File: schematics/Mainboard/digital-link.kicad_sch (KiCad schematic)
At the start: 1 part, among them J5 PCIE-036-02-X-D-TH

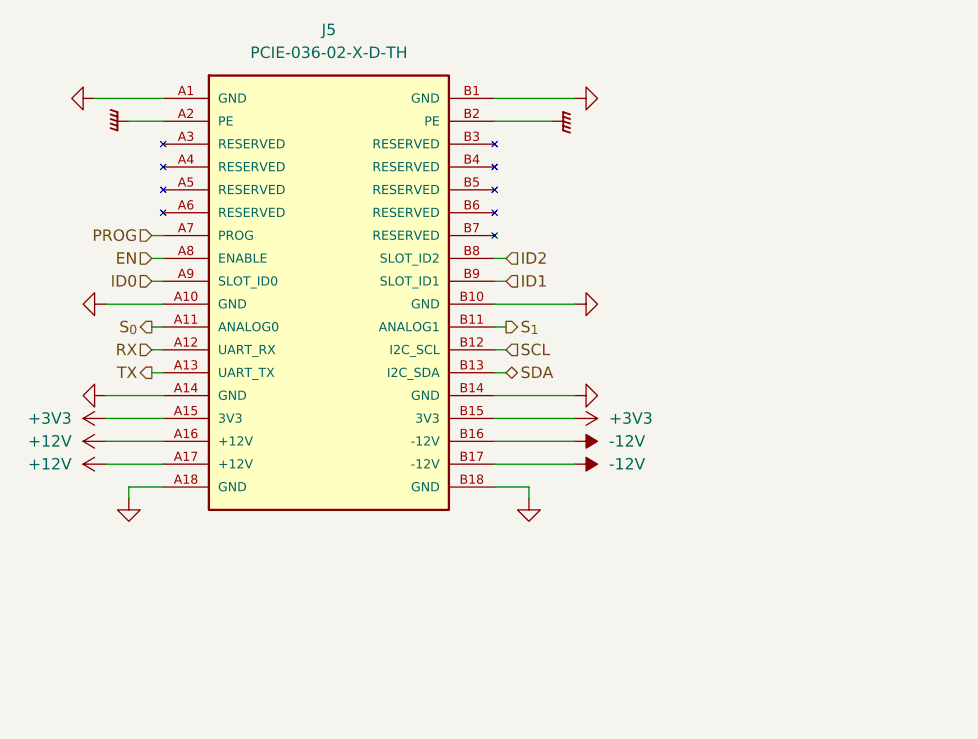
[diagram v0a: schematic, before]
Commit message: feat(mainboard): Added MCU and link comm bus
Signed-off-by: Andrew Balmos <abalmos@purdue.edu>
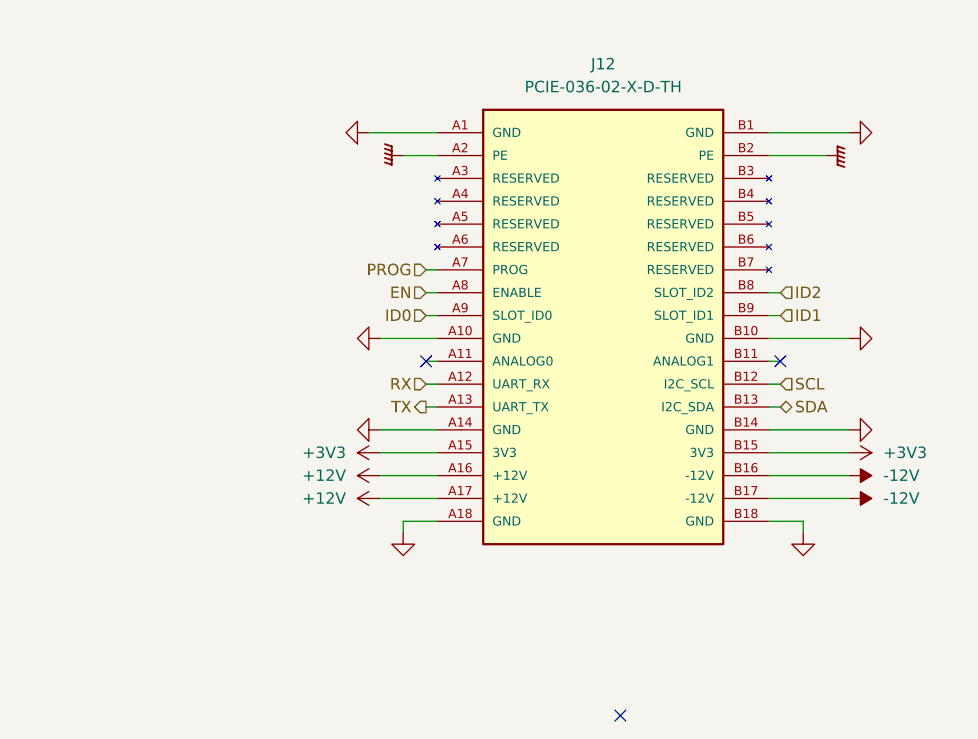
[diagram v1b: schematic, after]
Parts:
- removed J5: PCIE-036-02-X-D-TH, PCIE-036-02-X-D-TH:SAMTEC_PCIE-036-02-X-D-TH, symbol link-components:link-edge-connector
- added J12: PCIE-036-02-X-D-TH, PCIE-036-02-X-D-TH:SAMTEC_PCIE-036-02-X-D-TH, symbol link-components:link-edge-connector
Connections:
- net +12V: now also J12.A16 (+12V), J12.A17 (+12V)
- net +3V3: now also J12.A15 (3V3), J12.B15 (3V3)
- net -12V: now also J12.B16 (-12V), J12.B17 (-12V)
- net EN: now also J12.A8 (ENABLE)
- net GND: now also J12.A1 (GND), J12.A10 (GND), J12.A14 (GND), J12.A18 (GND), J12.B1 (GND), J12.B10 (GND), J12.B14 (GND), J12.B18 (GND)
- net GNDPWR: now also J12.A2 (PE), J12.B2 (PE)
- net ID0: now also J12.A9 (SLOT_ID0)
- net ID1: now also J12.B9 (SLOT_ID1)
- net ID2: now also J12.B8 (SLOT_ID2)
- net PROG: now also J12.A7 (PROG)
- net RX: now also J12.A12 (UART_RX)
- net SCL: now also J12.B12 (I2C_SCL)
- net SDA: now also J12.B13 (I2C_SDA)
- net TX: now also J12.A13 (UART_TX)
- no-connect marks 0 -> 3

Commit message: bug(labels): Fixed some incorrect labels
Signed-off-by: Andrew Balmos <abalmos@purdue.edu>
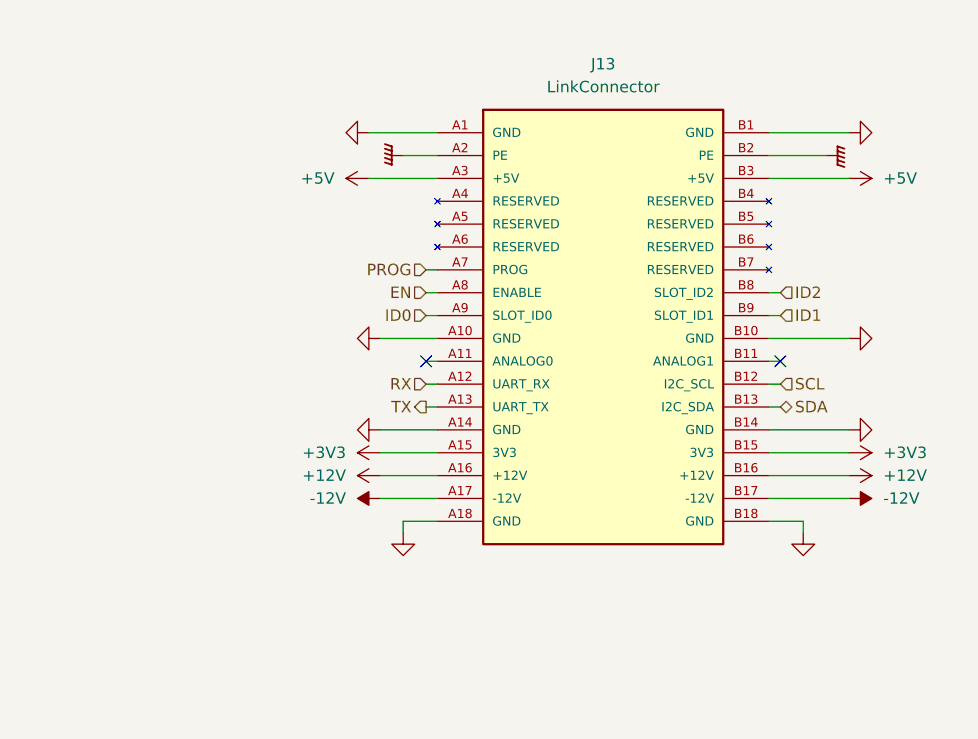
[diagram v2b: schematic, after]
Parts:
- J13: renamed from J12; value PCIE-036-02-X-D-TH -> LinkConnector
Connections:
- net +12V: now also J13.B16 (+12V); no longer J13.A17 (+12V)
- net -12V: now also J13.A17 (-12V); no longer J13.B16 (-12V)
- net +5V: now reaches J13.A3 (+5V)
- net +5V: now also J13.B3 (+5V)
- no-connect marks 3 -> 2

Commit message: bug(pcb): Link connector updates
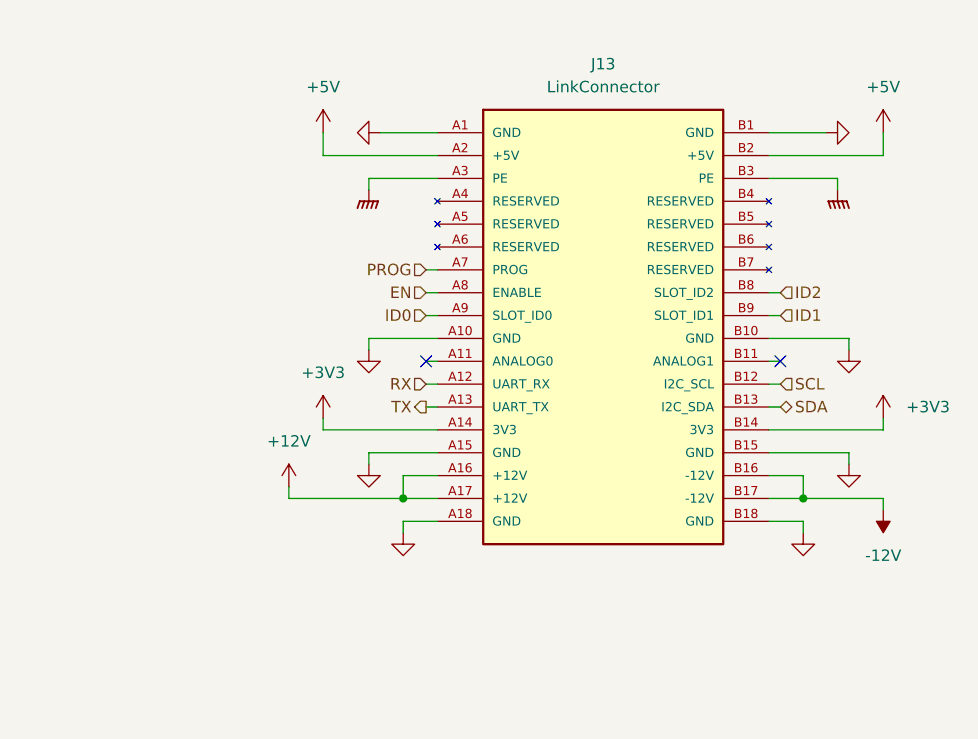
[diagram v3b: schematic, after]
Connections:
- net +12V: now also J13.A17 (+12V); no longer J13.B16 (+12V)
- net +3V3: now also J13.A14 (3V3), J13.B14 (3V3); no longer J13.A15 (3V3), J13.B15 (3V3)
- net +5V: now also J13.A2 (+5V), J13.B2 (+5V); no longer J13.A3 (+5V), J13.B3 (+5V)
- net -12V: now also J13.B16 (-12V); no longer J13.A17 (-12V)
- net GND: now also J13.A15 (GND), J13.B15 (GND); no longer J13.A14 (GND), J13.B14 (GND)
- net GNDPWR: now also J13.A3 (PE), J13.B3 (PE); no longer J13.A2 (PE), J13.B2 (PE)

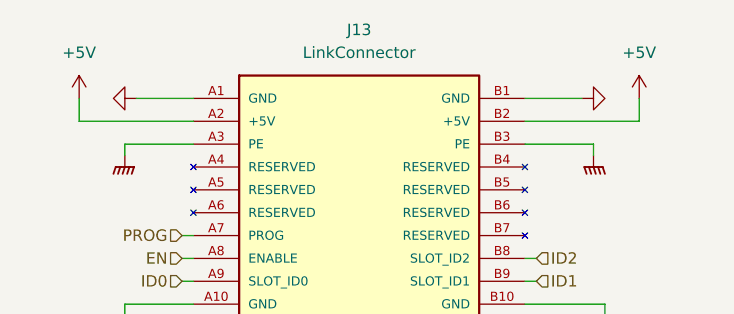
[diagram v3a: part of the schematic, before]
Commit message: feat(mainboard): Finished mainboard part selection
Signed-off-by: Andrew Balmos <abalmos@purdue.edu>
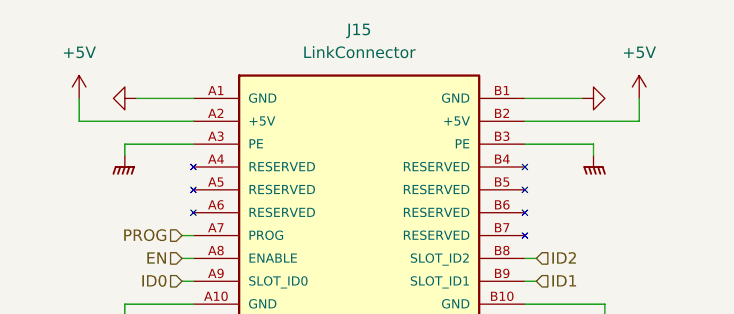
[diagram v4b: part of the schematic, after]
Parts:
- J15: renamed from J13; footprint PCIE-036-02-X-D-TH:SAMTEC_PCIE-036-02-X-D-TH -> Link_Footprints:SAMTEC_PCIE-036-02-X-D-TH; DigiKey (none) -> SAM10625-ND; LCSC (none) -> C194068; MPN (none) -> PCIE-036-02-F-D-TH
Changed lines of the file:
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@@
 		(dnp no)
 		(fields_autoplaced yes)
-		(property "Reference" "#PWR0171"
+		(property "Reference" "#PWR0213"
 			(at 116.84 100.33 0)
 			(effects
@@
 			(project "Mainboard"
 				(path "/95469dea-851e-4724-988e-7a6acaa4cbf0/4d738d37-6463-438f-b983-18ca4c02b52a"
-					(reference "#PWR0171")
+					(reference "#PWR0213")
 					(unit 1)
 				)
@@
 		(dnp no)
 		(fields_autoplaced yes)
-		(property "Reference" "#PWR0195"
+		(property "Reference" "#PWR0224"
 			(at 179.07 68.58 0)
 			(effects
@@
 			(project "Mainboard"
 				(path "/95469dea-851e-4724-988e-7a6acaa4cbf0/4d738d37-6463-438f-b983-18ca4c02b52a"
-					(reference "#PWR0195")
+					(reference "#PWR0224")
 					(unit 1)
 				)
@@
 		(dnp no)
 		(fields_autoplaced yes)
-		(property "Reference" "#PWR0190"
+		(property "Reference" "#PWR0222"
 			(at 175.26 95.25 0)
 			(effects
@@
 			(project "Mainboard"
 				(path "/95469dea-851e-4724-988e-7a6acaa4cbf0/4d738d37-6463-438f-b983-18ca4c02b52a"
-					(reference "#PWR0190")
+					(reference "#PWR0222")
 					(unit 1)
 				)
@@
 		(dnp no)
 		(fields_autoplaced yes)
-		(property "Reference" "#PWR0177"
+		(property "Reference" "#PWR0216"
 			(at 121.92 107.95 0)
 			(effects
@@
 			(project "Mainboard"
 				(path "/95469dea-851e-4724-988e-7a6acaa4cbf0/4d738d37-6463-438f-b983-18ca4c02b52a"
-					(reference "#PWR0177")
+					(reference "#PWR0216")
 					(unit 1)
 				)
@@
 		(dnp no)
 		(fields_autoplaced yes)
-		(property "Reference" "#PWR0188"
+		(property "Reference" "#PWR0220"
 			(at 179.07 64.77 0)
 			(effects
@@
 			(project "Mainboard"
 				(path "/95469dea-851e-4724-988e-7a6acaa4cbf0/4d738d37-6463-438f-b983-18ca4c02b52a"
-					(reference "#PWR0188")
+					(reference "#PWR0220")
 					(unit 1)
 				)
@@
 		(dnp no)
 		(fields_autoplaced yes)
-		(property "Reference" "#PWR0184"
+		(property "Reference" "#PWR0219"
 			(at 170.18 115.57 0)
 			(effects
@@
 			(project "Mainboard"
 				(path "/95469dea-851e-4724-988e-7a6acaa4cbf0/4d738d37-6463-438f-b983-18ca4c02b52a"
-					(reference "#PWR0184")
+					(reference "#PWR0219")
 					(unit 1)
 				)
@@
 		(dnp no)
 		(fields_autoplaced yes)
-		(property "Reference" "#PWR0196"
+		(property "Reference" "#PWR0225"
 			(at 179.07 100.33 0)
 			(effects
@@
 			(project "Mainboard"
 				(path "/95469dea-851e-4724-988e-7a6acaa4cbf0/4d738d37-6463-438f-b983-18ca4c02b52a"
-					(reference "#PWR0196")
+					(reference "#PWR0225")
 					(unit 1)
 				)
@@
 		(dnp no)
 		(fields_autoplaced yes)
-		(property "Reference" "#PWR0170"
+		(property "Reference" "#PWR0212"
 			(at 116.84 68.58 0)
 			(effects
@@
 			(project "Mainboard"
 				(path "/95469dea-851e-4724-988e-7a6acaa4cbf0/4d738d37-6463-438f-b983-18ca4c02b52a"
-					(reference "#PWR0170")
+					(reference "#PWR0212")
 					(unit 1)
 				)
@@
 		(dnp no)
 		(fields_autoplaced yes)
-		(property "Reference" "#PWR0194"
+		(property "Reference" "#PWR0223"
 			(at 175.26 107.95 0)
 			(effects
@@
 			(project "Mainboard"
 				(path "/95469dea-851e-4724-988e-7a6acaa4cbf0/4d738d37-6463-438f-b983-18ca4c02b52a"
-					(reference "#PWR0194")
+					(reference "#PWR0223")
 					(unit 1)
 				)
@@
 		(dnp no)
 		(fields_autoplaced yes)
-		(property "Reference" "#PWR0183"
+		(property "Reference" "#PWR0218"
 			(at 125.73 115.57 0)
 			(effects
@@
 			(project "Mainboard"
 				(path "/95469dea-851e-4724-988e-7a6acaa4cbf0/4d738d37-6463-438f-b983-18ca4c02b52a"
-					(reference "#PWR0183")
+					(reference "#PWR0218")
 					(unit 1)
 				)
@@
 		(dnp no)
 		(fields_autoplaced yes)
-		(property "Reference" "#PWR0172"
+		(property "Reference" "#PWR0214"
 			(at 121.92 76.2 0)
 			(effects
@@
 			(project "Mainboard"
 				(path "/95469dea-851e-4724-988e-7a6acaa4cbf0/4d738d37-6463-438f-b983-18ca4c02b52a"
-					(reference "#PWR0172")
+					(reference "#PWR0214")
 					(unit 1)
 				)
@@
 		(dnp no)
 		(fields_autoplaced yes)
-		(property "Reference" "#PWR0178"
+		(property "Reference" "#PWR0217"
 			(at 116.84 64.77 0)
 			(effects
@@
 			(project "Mainboard"
 				(path "/95469dea-851e-4724-988e-7a6acaa4cbf0/4d738d37-6463-438f-b983-18ca4c02b52a"
-					(reference "#PWR0178")
+					(reference "#PWR0217")
 					(unit 1)
 				)
@@
 		(dnp no)
 		(fields_autoplaced yes)
-		(property "Reference" "J13"
+		(property "Reference" "J15"
 			(at 147.955 57.15 0)
 			(effects
@@
 			)
 		)
-		(property "Footprint" "PCIE-036-02-X-D-TH:SAMTEC_PCIE-036-02-X-D-TH"
+		(property "Footprint" "Link_Footprints:SAMTEC_PCIE-036-02-X-D-TH"
 			(at 148.59 87.63 0)
 			(effects
@@
 			)
 		)
+		(property "LCSC" "C194068"
+			(at 148.59 87.63 0)
+			(effects
+				(font
+					(size 1.27 1.27)
+				)
+				(hide yes)
+			)
+		)
+		(property "MPN" "PCIE-036-02-F-D-TH"
+			(at 148.59 87.63 0)
+			(effects
+				(font
+					(size 1.27 1.27)
+				)
+				(hide yes)
+			)
+		)
+		(property "DigiKey" "SAM10625-ND"
+			(at 148.59 87.63 0)
+			(effects
+				(font
+					(size 1.27 1.27)
+				)
+				(hide yes)
+			)
+		)
 		(pin "A17"
 		)
@@
 			(project "Mainboard"
 				(path "/95469dea-851e-4724-988e-7a6acaa4cbf0/4d738d37-6463-438f-b983-18ca4c02b52a"
-					(reference "J13")
+					(reference "J15")
 					(unit 1)
 				)
@@
 		(dnp no)
 		(fields_autoplaced yes)
-		(property "Reference" "#PWR0166"
+		(property "Reference" "#PWR0211"
 			(at 113.03 107.95 0)
 			(effects
@@
 			(project "Mainboard"
 				(path "/95469dea-851e-4724-988e-7a6acaa4cbf0/4d738d37-6463-438f-b983-18ca4c02b52a"
-					(reference "#PWR0166")
+					(reference "#PWR0211")
 					(unit 1)
 				)
@@
 		(dnp no)
 		(fields_autoplaced yes)
-		(property "Reference" "#PWR0197"
+		(property "Reference" "#PWR0226"
 			(at 179.07 102.87 0)
 			(effects
@@
 			(project "Mainboard"
 				(path "/95469dea-851e-4724-988e-7a6acaa4cbf0/4d738d37-6463-438f-b983-18ca4c02b52a"
-					(reference "#PWR0197")
+					(reference "#PWR0226")
 					(unit 1)
 				)
@@
 		(dnp no)
 		(fields_autoplaced yes)
-		(property "Reference" "#PWR0176"
+		(property "Reference" "#PWR0215"
 			(at 121.92 95.25 0)
 			(effects
@@
 			(project "Mainboard"
 				(path "/95469dea-851e-4724-988e-7a6acaa4cbf0/4d738d37-6463-438f-b983-18ca4c02b52a"
-					(reference "#PWR0176")
+					(reference "#PWR0215")
 					(unit 1)
 				)
@@
 		(dnp no)
 		(fields_autoplaced yes)
-		(property "Reference" "#PWR0189"
+		(property "Reference" "#PWR0221"
 			(at 173.99 76.2 0)
 			(effects
@@
 			(project "Mainboard"
 				(path "/95469dea-851e-4724-988e-7a6acaa4cbf0/4d738d37-6463-438f-b983-18ca4c02b52a"
-					(reference "#PWR0189")
-					(unit 1)
-				)
+					(reference "#PWR0221")
+					(unit 1)
+				)

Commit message: release(mainboard): v1.0. Ordered.
Signed-off-by: Andrew Balmos <abalmos@purdue.edu>
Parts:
- J15: FT Position Offset (none) -> 1.2065,0
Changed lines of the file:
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@@
+			)
+		)
+		(property "FT Position Offset" "1.2065,0"
+			(at 148.59 87.63 0)
+			(effects
+				(font
+					(size 1.27 1.27)
+				)
+				(hide yes)
 			)
 		)
